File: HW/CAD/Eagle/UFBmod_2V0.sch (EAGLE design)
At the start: 189 parts, among them T0551 MMBT2222, U0501 MIDAS_MCCOG21605B6W-FPTLWI, U0601 MAX5217, U0701 AT86RF215-ZU, U0711 ASVTX-13-D-26.000MHZ-I05-T, U0811 PE4259, U0821 RFX1010, U0881 B39871B3440U410, U0911 FT232HL, U1101 TPS53353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

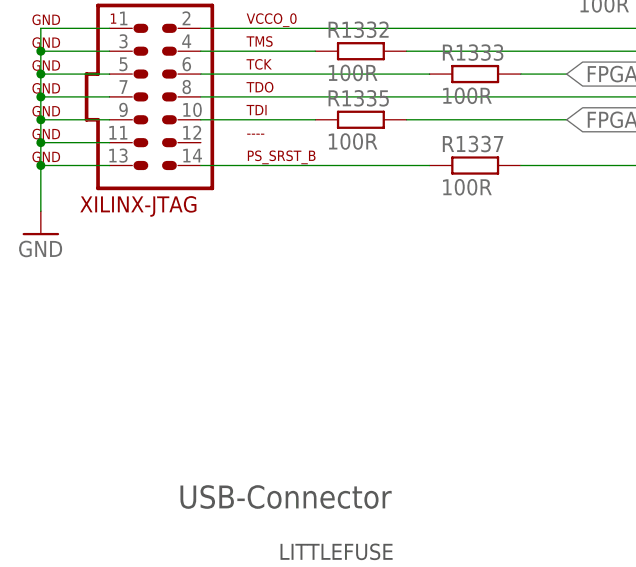
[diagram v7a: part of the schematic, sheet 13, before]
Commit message: HW - CAD/Eagle - JTAG programmer info added
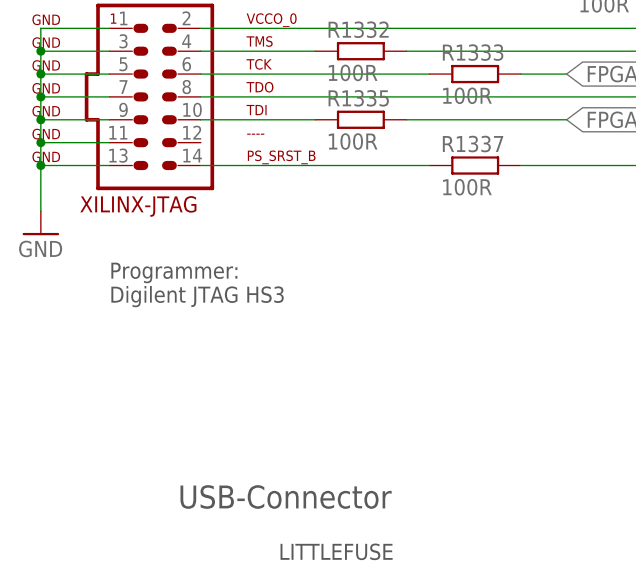
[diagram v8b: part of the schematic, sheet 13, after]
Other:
- note added: "Programmer: Digilent JTAG HS3"
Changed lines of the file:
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@@
 <text x="22.86" y="73.66" size="2.54" layer="97" ratio="15">USB-Connector</text>
 <text x="50.8" y="154.94" size="1.778" layer="97">JTAG CPLD EN</text>
+<text x="15.24" y="96.52" size="1.778" layer="97">Programmer:
+Digilent JTAG HS3</text>
 </plain>
 <instances>
